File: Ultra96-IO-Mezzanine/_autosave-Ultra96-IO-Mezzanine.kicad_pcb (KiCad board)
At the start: 2 copper layers, 85 x 54 mm, 43 parts, among them J1 USB_C_Receptacle_USB2.0, J2 Conn_01x08_Female, J3 USB_C_Receptacle_USB2.0, P1 CONN_02X20, P2 CONN_02X30, P3 CONN_02X20, Q1 STL6P3LLH6, SW1 SW_SP3T, U1 TXS0104ERGYR, U2 CP2102N-A01-GQFN24, U3 TXS0108EPW, U4 STUSB4500QTR, U5 TXS0108EPW

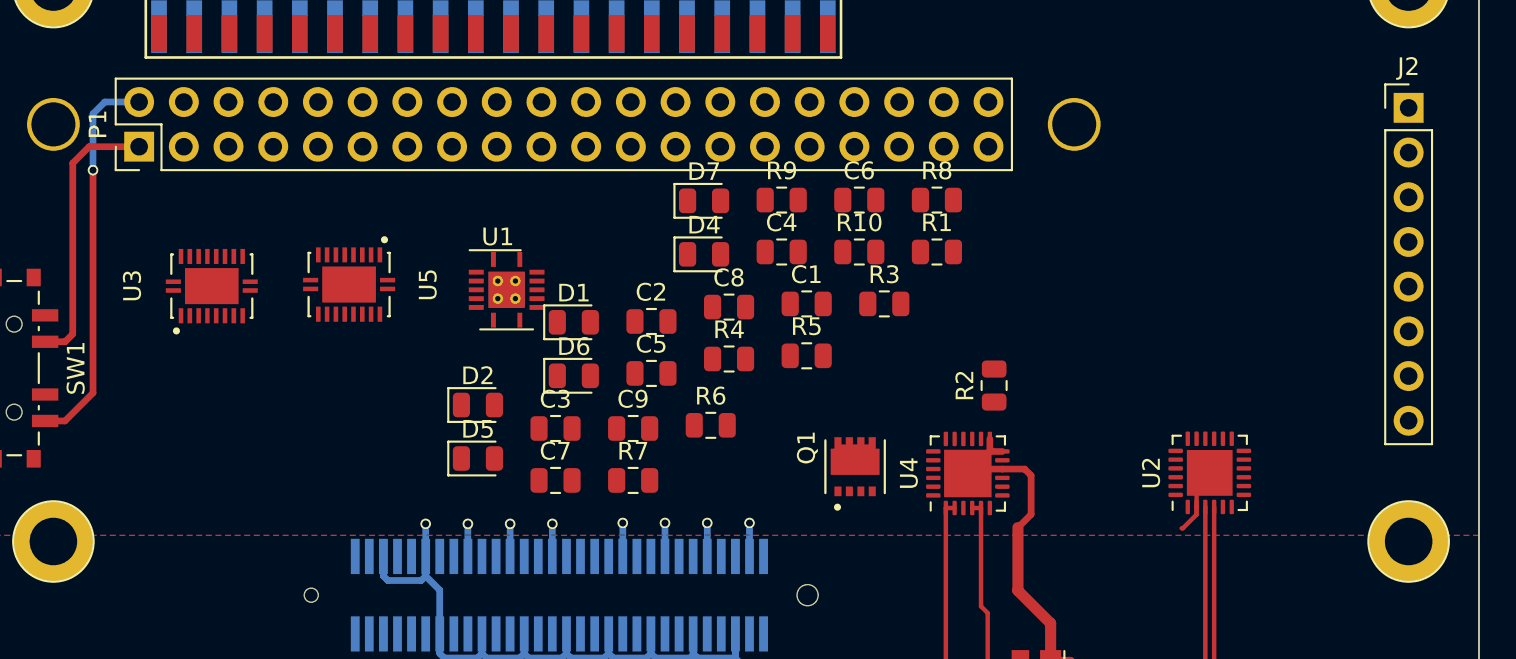
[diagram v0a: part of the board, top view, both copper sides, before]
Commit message: Added TXS0108
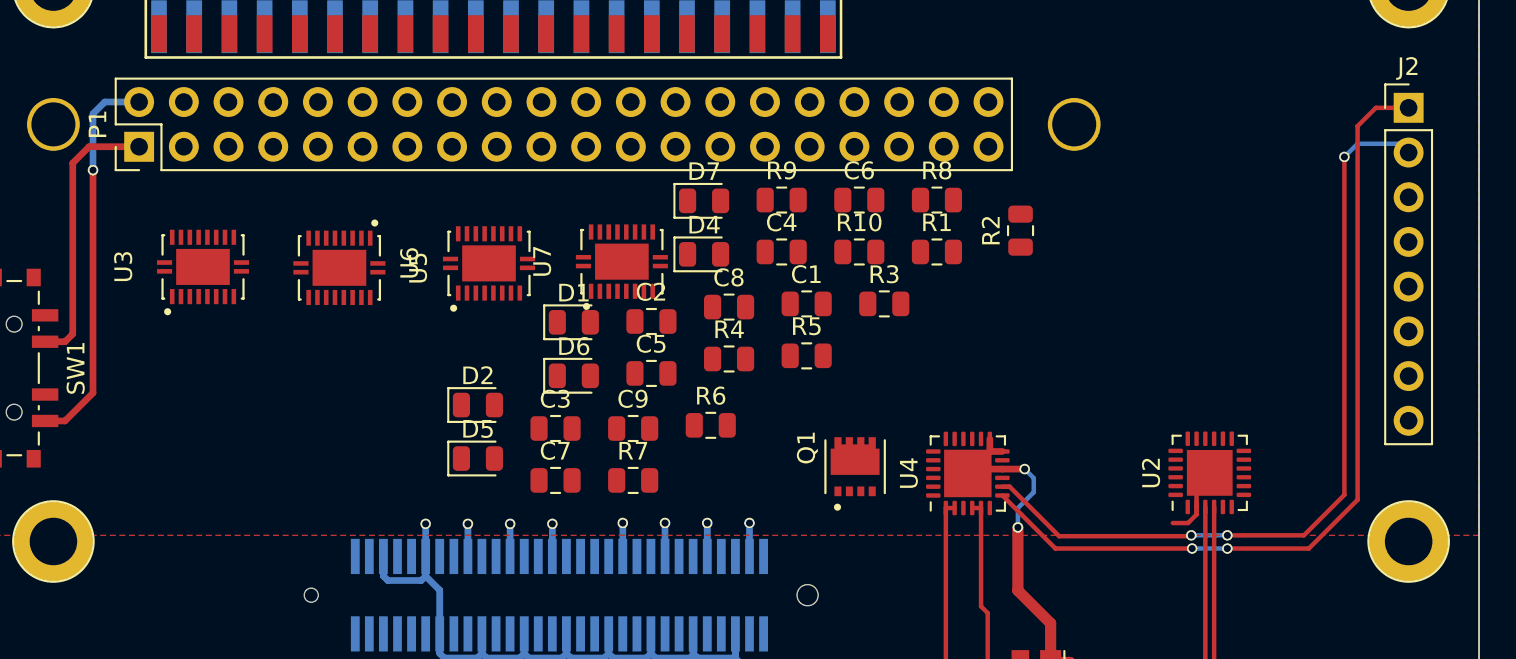
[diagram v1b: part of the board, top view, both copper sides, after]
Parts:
- removed U1: TXS0104ERGYR, Package_DFN_QFN:Texas_S-PVQFN-N14_ThermalVias
- added U6: TXS0108EPW, LevelShifter:QFN50P450X350X100-21N, F.Cu at (128.8, 119.7)
- added U7: TXS0108EPW, LevelShifter:QFN50P450X350X100-21N, F.Cu at (136.3, 119.6)
- moved R2 8.93 mm to (158.9, 117.8)
- moved U3 1.20 mm to (112.5, 119.9)
- moved U5 1.10 mm to (120.2, 120.0)
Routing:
- net I2C0_SCL_RPI: track 0.00 -> 47.1 mm, vias 0 -> 2
- net I2C0_SDA_RPI: track 0.00 -> 44.9 mm, vias 0 -> 3
- net GND: track 148.2 -> 148.7 mm, vias 8 -> 10
